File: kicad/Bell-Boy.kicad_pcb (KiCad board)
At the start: 2 copper layers, 61 x 58.4 mm, 17 parts

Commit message: PCB and other updates
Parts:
- removed the 270R at (131.4, 78.7)
- removed the ? at (152.4, 109.2)
- removed the ? at (137.2, 109.2)
- added 270R: , Resistors_ThroughHole:Resistor_Horizontal_RM7mm, F.Cu at (130.8, 78.7)
- added ?: , Pin_Headers:Pin_Header_Straight_1x04, F.Cu at (151.1, 109.2)
- added ?: , Pin_Headers:Pin_Header_Straight_1x04, F.Cu at (121.4, 119.9)
- 4K7: footprint Resistors_ThroughHole:Resistor_Horizontal_RM10mm -> Resistors_ThroughHole:Resistor_Horizontal_RM7mm
- ?: value (none) -> RPi Header
- moved ? 5.52 mm to (136.5, 73.7), turned to 0 degrees
- moved ? 3.31 mm to (133.9, 65.0)
- moved ? 1.27 mm to (163.8, 66.0)
- moved ? 1.27 mm to (161.3, 104.1)
- moved ? 1.05 mm to (123.4, 65.0)
- moved ? 1.02 mm to (172.7, 110.2)
- moved ? 1.02 mm to (116.8, 110.2)
- moved 4K7 0.64 mm to (133.3, 78.7)
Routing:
- net Net-(P1-Pad2): track 98.3 -> 111.0 mm
- net Net-(P1-Pad6): track 80.0 -> 92.4 mm
- net GND: track 29.3 -> 17.3 mm
- net Net-(D2-Pad2): track 24.9 -> 14.0 mm
- net Net-(D3-Pad2): track 50.5 -> 56.4 mm
- net Net-(P1-Pad5): track 81.3 -> 86.4 mm
- net Net-(P1-Pad3): track 91.4 -> 86.4 mm
- net Net-(P4-Pad1): track 22.7 -> 19.3 mm
- net Net-(D1-Pad1): track 24.8 -> 27.6 mm, vias 1 -> 0
- net Net-(D1-Pad2): track 17.2 -> 15.2 mm
- net Net-(D4-Pad1): track 47.6 -> 48.7 mm
- net Net-(D2-Pad1): track 25.7 -> 24.7 mm
- net +3V3: track 49.3 -> 50.2 mm
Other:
- outline, holes or cut-outs redrawn
- board text added: "+"
- board text added: "-"
- board text added: "GY-521"
- board text added: "NXP"
- board text added: "TOP SIDE"

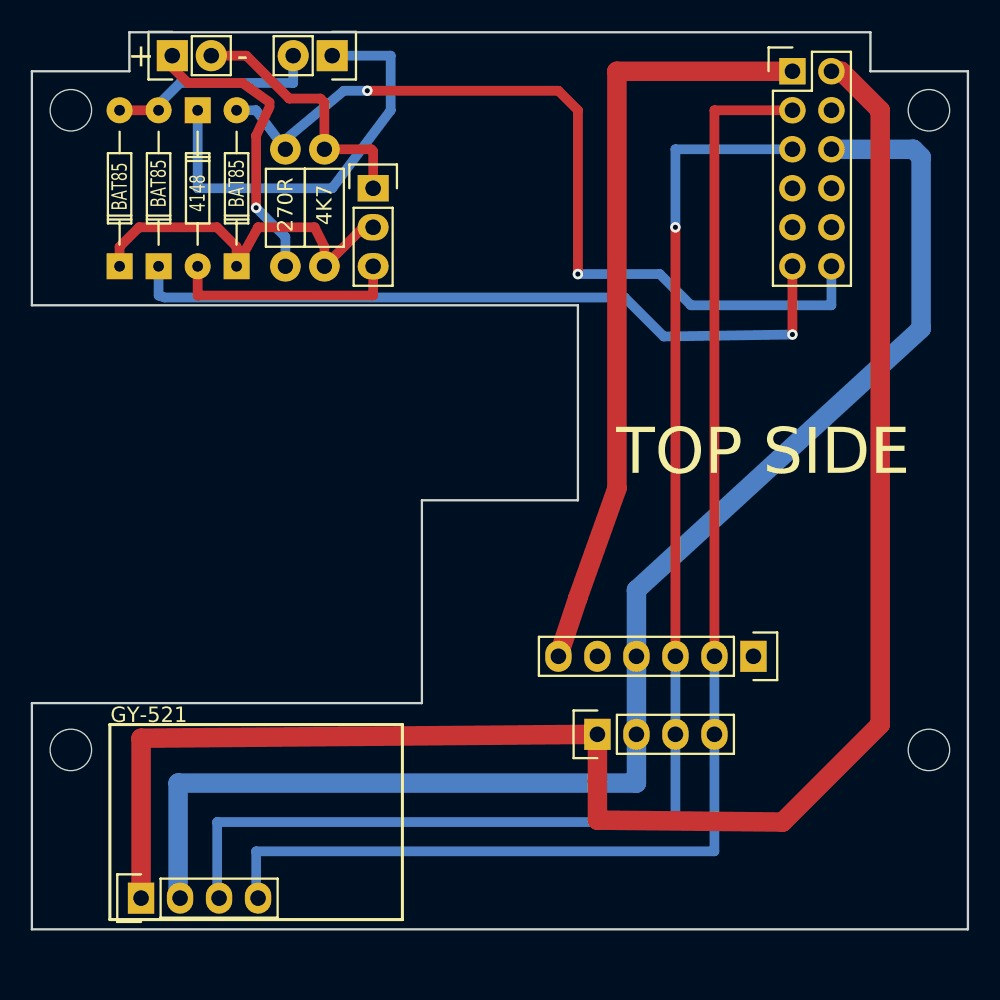
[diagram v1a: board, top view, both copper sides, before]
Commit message: Automated all calibration.  Updated PCB
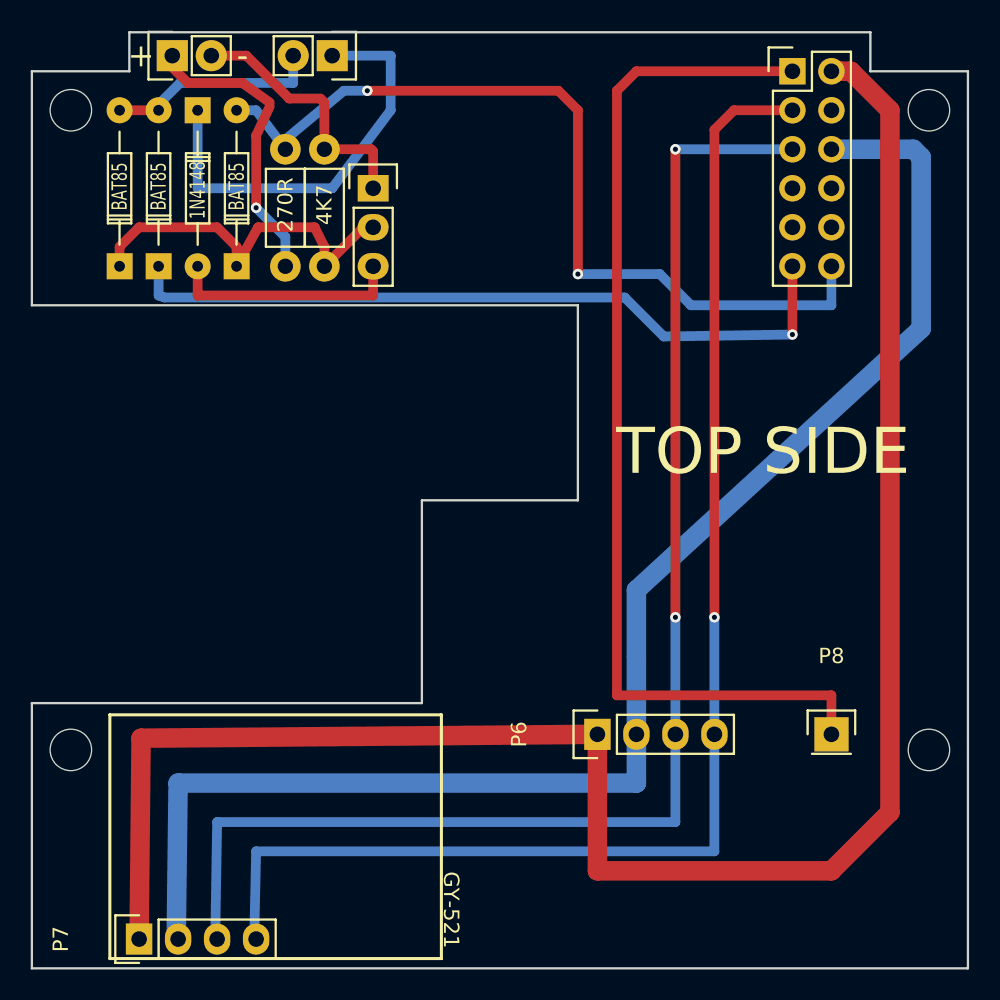
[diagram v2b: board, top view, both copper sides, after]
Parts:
- removed the ? at (172.7, 68.6)
- removed the ? at (116.8, 68.6)
- removed the ? at (161.3, 104.1)
- removed the ? at (172.7, 110.2)
- removed the ? at (116.8, 110.2)
- added ? (x2): , Mounting_Holes:MountingHole_2.7mm, F.Cu at (172.7, 68.6)
- added ?: , Mounting_Holes:MountingHole_2.7mm, F.Cu at (116.8, 68.6)
- added ?: , Mounting_Holes:MountingHole_2.7mm, F.Cu at (116.8, 110.2)
- added ?: , Mounting_Holes:MountingHole_2.7mm, F.Cu at (172.7, 110.2)
- added P8: AD0, Pin_Headers:Pin_Header_Straight_1x01, F.Cu at (166.4, 109.2)
- P6, P7: renamed from ?; value (none) -> MPU6050
- moved P7 2.67 mm to (121.3, 122.6)
- renumbered 4148 to 1N4148
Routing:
- net +3V3: track 50.2 -> 67.8 mm
- net Net-(P1-Pad2): track 111.0 -> 123.5 mm
- net Net-(P1-Pad5): track 86.4 -> 89.0 mm, vias 1 -> 2
- net Net-(P1-Pad6): track 92.4 -> 95.1 mm
- net Net-(P1-Pad3): track 86.4 -> 88.3 mm, vias 0 -> 1
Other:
- board size 61 x 58.4 mm -> 61 x 61 mm
- board text removed: "NXP"
